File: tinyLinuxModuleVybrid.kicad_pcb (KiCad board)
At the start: 4 copper layers, 171 parts, among them IC201 LAN8720, IC401 WM-294, IC501 USB2514B, IC502 WE-TVS-82400274, IC503 TPS2033, IC504 WE-TVS-82400274, IC801 BME680, M102 SCREW, M104 SCREW, M106 SCREW, M108 SCREW, Q101 2N7002BKT, Q102 2N7002BKT, Q103 2N7002BKT, Q301 2N7002BKT, U301 U-BLOX-TOBY-L2, U401 U-BLOX_LILY-W1, U601 U-BLOX-NEO-M8N, U801 MPU-9250, X101 MICROSD, X102 LAN_Transformer, X103 CONN_01x06, X104 VybridBoard, X105 ARM_JTAG_10, X301 ANT, X302 SIMcard, X303 ANT, X401 ANT, X601 ANT, Y501 24M,18p

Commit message: adjusted 3d models
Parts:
- added IC704: TPS82085, Switcher_IC:TPS82085, F.Cu at (184.3, 74.0)
- added IC705: TPS82085, Switcher_IC:TPS82085, F.Cu at (184.3, 77.3)
- added L801: B, Passives:B0402N, F.Cu at (185.1, 20.7)
- added LED104: G, Passives:LED0603N, F.Cu at (163.5, 68.7)
- added LED105: Y, Passives:LED0603N, F.Cu at (163.7, 65.8)
- added LED601: G, Passives:LED0603N, F.Cu at (183.5, 46.1)
- added Q601: 2N7002BKT, Transistor:SOT416_GSD, F.Cu at (166.8, 57.2)
- added R605: 1k, Passives:R0402N, F.Cu at (192.5, 25.4)
- added U802: LMT86, Sensors:R-PDSO-G5, F.Cu at (188.2, 73.4)
- X103: footprint Connector:MLX127_53398_SMD-06 -> Connector:PicoLock_6
- moved M102 271.5 mm to (236.4, 133.5)
- moved X601 267.2 mm to (234.6, 127.9)
- moved X301 262.0 mm to (238.2, 109.1)
- moved M106 254.9 mm to (236.4, 95.4)
- moved C205 247.8 mm to (241.9, 53.5)
- moved U801 238.3 mm to (228.2, 68.7)
- moved C206 233.5 mm to (219.6, 79.4)
- moved C204 233.4 mm to (227.5, 52.2)
- moved R207 230.3 mm to (219.6, 69.5)
- moved Q101 230.1 mm to (217.8, 74.1)
- moved R206 229.0 mm to (219.4, 65.7)
- moved R209 228.2 mm to (214.5, 77.8)
- moved R201 227.0 mm to (216.6, 67.9)
- moved R205 226.9 mm to (218.3, 61.6)
- moved R208 225.3 mm to (212.0, 76.3)
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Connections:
- net /Communication/NEO/USB_DM renamed Net-(U601-Pad6)
- net /Communication/NEO/USB_DP renamed Net-(U601-Pad5)
- net /Communication/RMII_CRSDV renamed /PTC11
- net /Communication/RMII_MDC renamed /PTC9
- net /Communication/RMII_MDIO renamed /PTC10
- net /Communication/RMII_REFCLK renamed /PTA6
- net /Communication/RMII_RX0 renamed /PTC13
- net /Communication/RMII_RX1 renamed /PTC12
- net /Communication/RMII_RXER renamed /PTC14
- net /Communication/RMII_TX0 renamed /PTC16
- net /Communication/RMII_TX1 renamed /PTC15
- net /Communication/RMII_TXEN renamed /PTC17
- net /Communication/USB_D+ renamed /USB0_D_P
- net /Communication/USB_D- renamed /USB0_D_N
- net /Communication/~RESET renamed /~RESET
- X104 pad M1: Net-(X104-PadM1) -> GND
- X104 pad M2: Net-(X104-PadM2) -> GND
- X104 pad M3: Net-(X104-PadM3) -> GND
- X104 pad M4: Net-(X104-PadM4) -> GND
- X104 pad M5: Net-(X104-PadM5) -> GND
- X104 pad M6: Net-(X104-PadM6) -> GND
- X104 pad M7: Net-(X104-PadM7) -> GND
- X104 pad M8: Net-(X104-PadM8) -> GND
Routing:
- net (no net): track 8.63 -> 279.4 mm
- removed copper zone on In2.Cu, net +3V3
- removed copper zone on In1.Cu, net GND
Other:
- board outline added: 91.4 x 48.3 mm

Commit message: sorted components
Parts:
- added C720: 10u, 10V, Passives:C0805N, F.Cu at (123.6, 44.3)
- added C721: 10u, 10V, Passives:C0805N, F.Cu at (113.4, 44.3)
- added C722: 22u, 3mOhm, Passives:C0805N, F.Cu at (126.1, 41.6)
- added C723: 22u, 3mOhm, Passives:C0805N, F.Cu at (116.2, 41.4)
- added G***: LOGO, Symbols:hsrm_logo, F.Cu at (233.8, 116.2)
- added R606: 10, Passives:R0402N, F.Cu at (195.7, 148.6)
- added REF**: Symbol_ESD-Logo_CopperTop, Symbols:Symbol_ESD-Logo_CopperTop, F.Cu at (217.1, 103.2)
- C308, C309, C311, C313, C315, D301, D302, D303, D304, D305: moved to B.Cu
- R304: value R -> 0
- X101: moved to F.Cu
- moved R117 148.0 mm to (155.4, 162.4)
- moved R116 146.4 mm to (155.3, 159.6)
- moved C205 142.2 mm to (164.7, 172.8)
- moved R602 141.3 mm to (122.3, 131.9), turned to 90 degrees
- moved C204 138.4 mm to (164.5, 175.4)
- moved R603 137.4 mm to (113.4, 131.4), turned to 180 degrees
- moved D101 137.1 mm to (155.4, 151.2)
- moved R120 136.0 mm to (153.6, 153.3)
- moved R119 132.1 mm to (156.4, 148.7)
- moved R604 131.9 mm to (123.6, 131.9), turned to 90 degrees
- moved R118 128.8 mm to (156.4, 153.3)
- moved C202 128.7 mm to (164.2, 181.7)
- moved R601 125.9 mm to (116.7, 115.7)
- moved R401 125.6 mm to (201.1, 159.1), turned to 90 degrees
- moved R121 125.6 mm to (153.6, 148.7)
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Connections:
- IC401 pad 8: /Communication/LILY/RF -> Net-(IC401-Pad8)
- IC704 pad P: (no net) -> GND
- IC705 pad P: (no net) -> GND
- U601 pad 20: (no net) -> Net-(R602-Pad1)
- U601 pad 22: Net-(R602-Pad1) -> +3V3
- U601 pad 3: Net-(Q601-PadG) -> Net-(R606-Pad1)
- X103 pad 1: Net-(X102-Pad16) -> Net-(X102-Pad9)
- X103 pad 2: Net-(R120-Pad1) -> Net-(R121-Pad1)
- X103 pad 3: Net-(X102-Pad14) -> Net-(X102-Pad11)
- X103 pad 4: Net-(X102-Pad11) -> Net-(X102-Pad14)
- X103 pad 5: Net-(R121-Pad1) -> Net-(R120-Pad1)
- X103 pad 6: Net-(X102-Pad9) -> Net-(X102-Pad16)

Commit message: sorted components
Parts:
- moved REF** 117.8 mm to (334.7, 95.6)
- moved G*** 96.0 mm to (323.8, 82.7)
- moved R603 86.7 mm to (200.1, 135.8), turned to 270 degrees
- moved R602 78.4 mm to (200.6, 126.9), turned to 180 degrees
- moved R604 77.2 mm to (200.6, 125.6), turned to 180 degrees
- moved C602 76.3 mm to (200.6, 124.6), turned to 0 degrees
- moved LED105 75.7 mm to (173.4, 90.0), turned to 270 degrees
- moved C601 75.4 mm to (200.6, 123.6), turned to 0 degrees
- moved LED104 73.9 mm to (176.2, 90.0), turned to 270 degrees
- moved U601 72.9 mm to (192.4, 129.4), turned to 180 degrees
- moved L601 72.4 mm to (184.3, 134.7), turned to 90 degrees
- moved X601 70.9 mm to (181.0, 135.2), turned to 90 degrees
- moved R117 70.7 mm to (173.4, 94.1), turned to 270 degrees
- moved R601 69.6 mm to (184.3, 132.5), turned to 90 degrees
- moved X103 69.6 mm to (184.8, 90.0), turned to 180 degrees
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
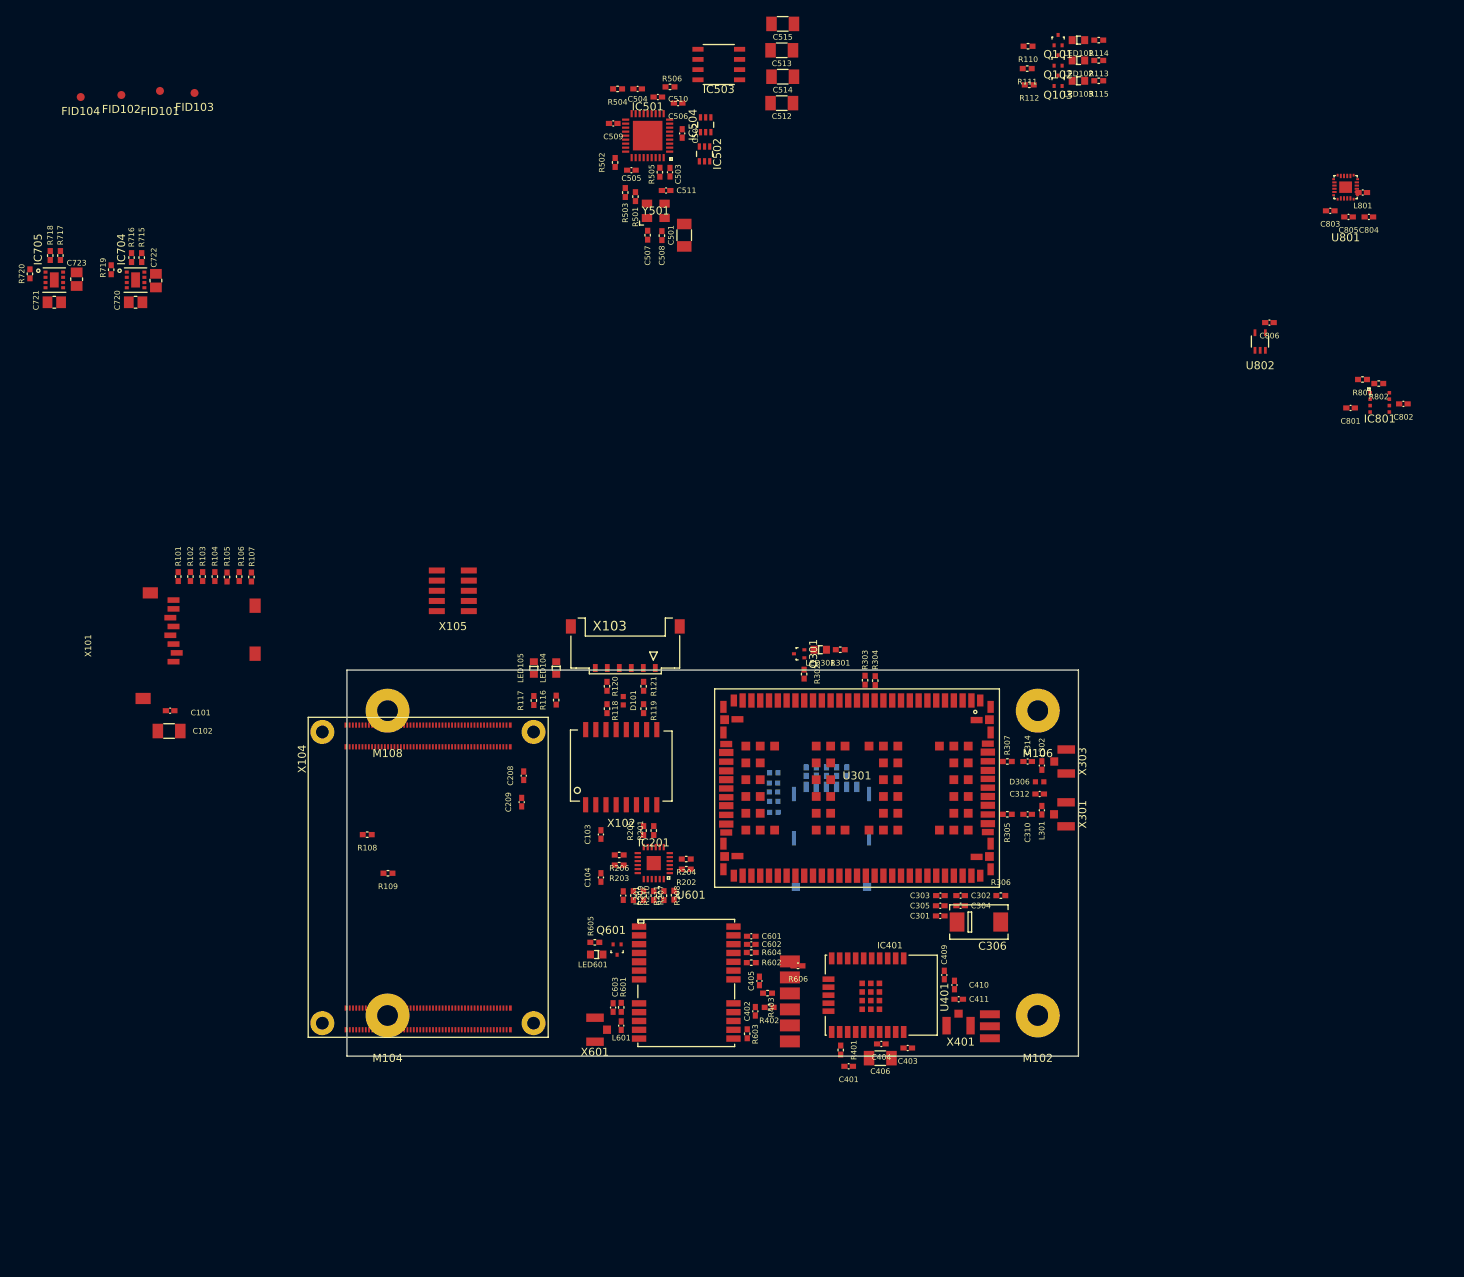
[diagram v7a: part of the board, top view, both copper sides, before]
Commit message: selected connector pins
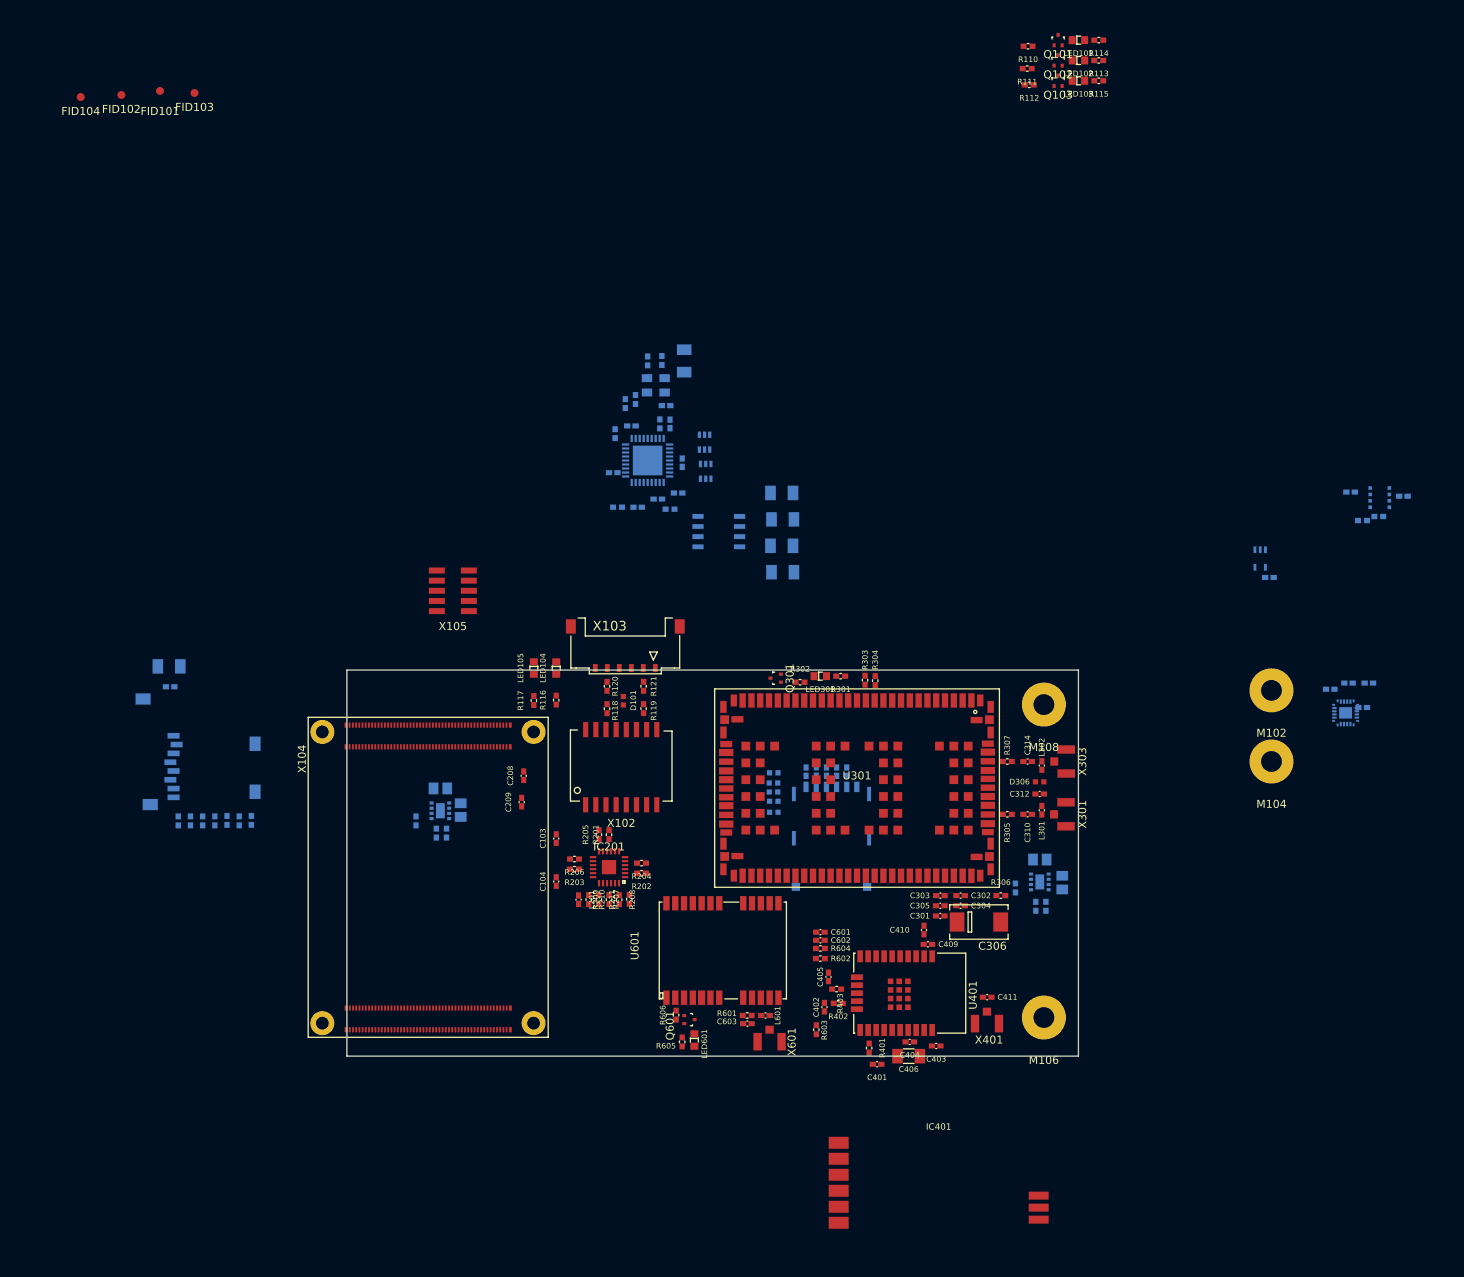
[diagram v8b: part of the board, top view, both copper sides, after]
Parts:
- removed R108, R109: 22, Passives:R0402N
- C101, C102, C501, C502, C503, C504, C505, C506, C507, C508, C509, C510, C511, C512, C513, C514, C515, C720, C721, C722, C723, C801, C802, C803, C804, C805, C806, IC501, IC502, IC503, IC504, IC704, IC705, IC801, L801, R101, R102, R103, R104, R105, R106, R107, R501, R502, R503, R504, R505, R506, R715, R716, R717, R718, R719, R720, R801, R802, U801, U802, X101, Y501: moved to B.Cu
- moved R718 147.6 mm to (236.1, 119.8), turned to 90 degrees
- moved R717 147.6 mm to (237.4, 119.8), turned to 270 degrees
- moved R720 145.2 mm to (233.6, 117.5), turned to 90 degrees
- moved C723 144.4 mm to (239.4, 116.9), turned to 90 degrees
- moved IC705 144.4 mm to (236.6, 116.8)
- moved C721 141.5 mm to (236.6, 114.0)
- moved M104 115.0 mm to (265.6, 101.7)
- moved M108 82.0 mm to (237.1, 94.6)
- moved R715 81.4 mm to (162.5, 110.7), turned to 270 degrees
- moved R716 81.4 mm to (161.2, 110.7), turned to 90 degrees
- moved R719 78.7 mm to (158.7, 109.2), turned to 90 degrees
- moved IC704 76.5 mm to (161.7, 107.9)
- moved C722 76.4 mm to (164.2, 107.8), turned to 90 degrees
- moved C720 71.7 mm to (161.7, 105.1)
- moved C515 68.5 mm to (204.5, 78.1)
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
